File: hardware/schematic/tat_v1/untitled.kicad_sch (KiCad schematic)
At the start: 26 parts, among them J2 USB_C_Receptacle_USB2.0_14P, J3 JST-PH 2 Pin, SW6 SW_SPDT, U5 BQ25185, U6 TPS631000DRLR, U7 USBLC6-2P6

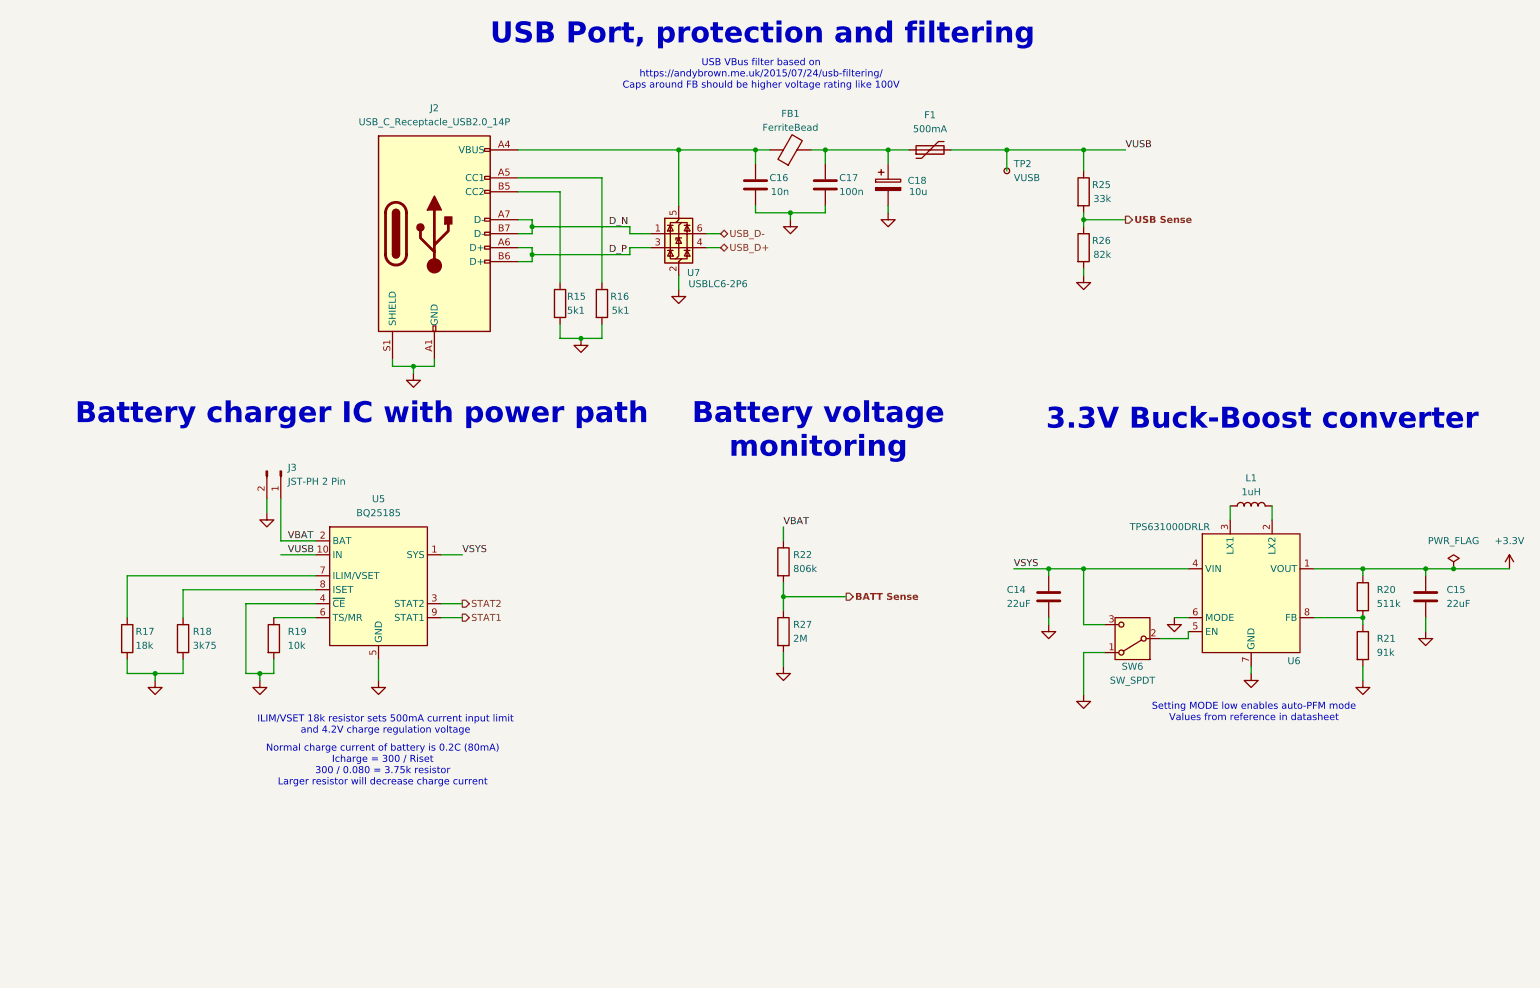
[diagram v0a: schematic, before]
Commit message: Cleaned up basic schematic and double checked all components. Need to complete ERC.
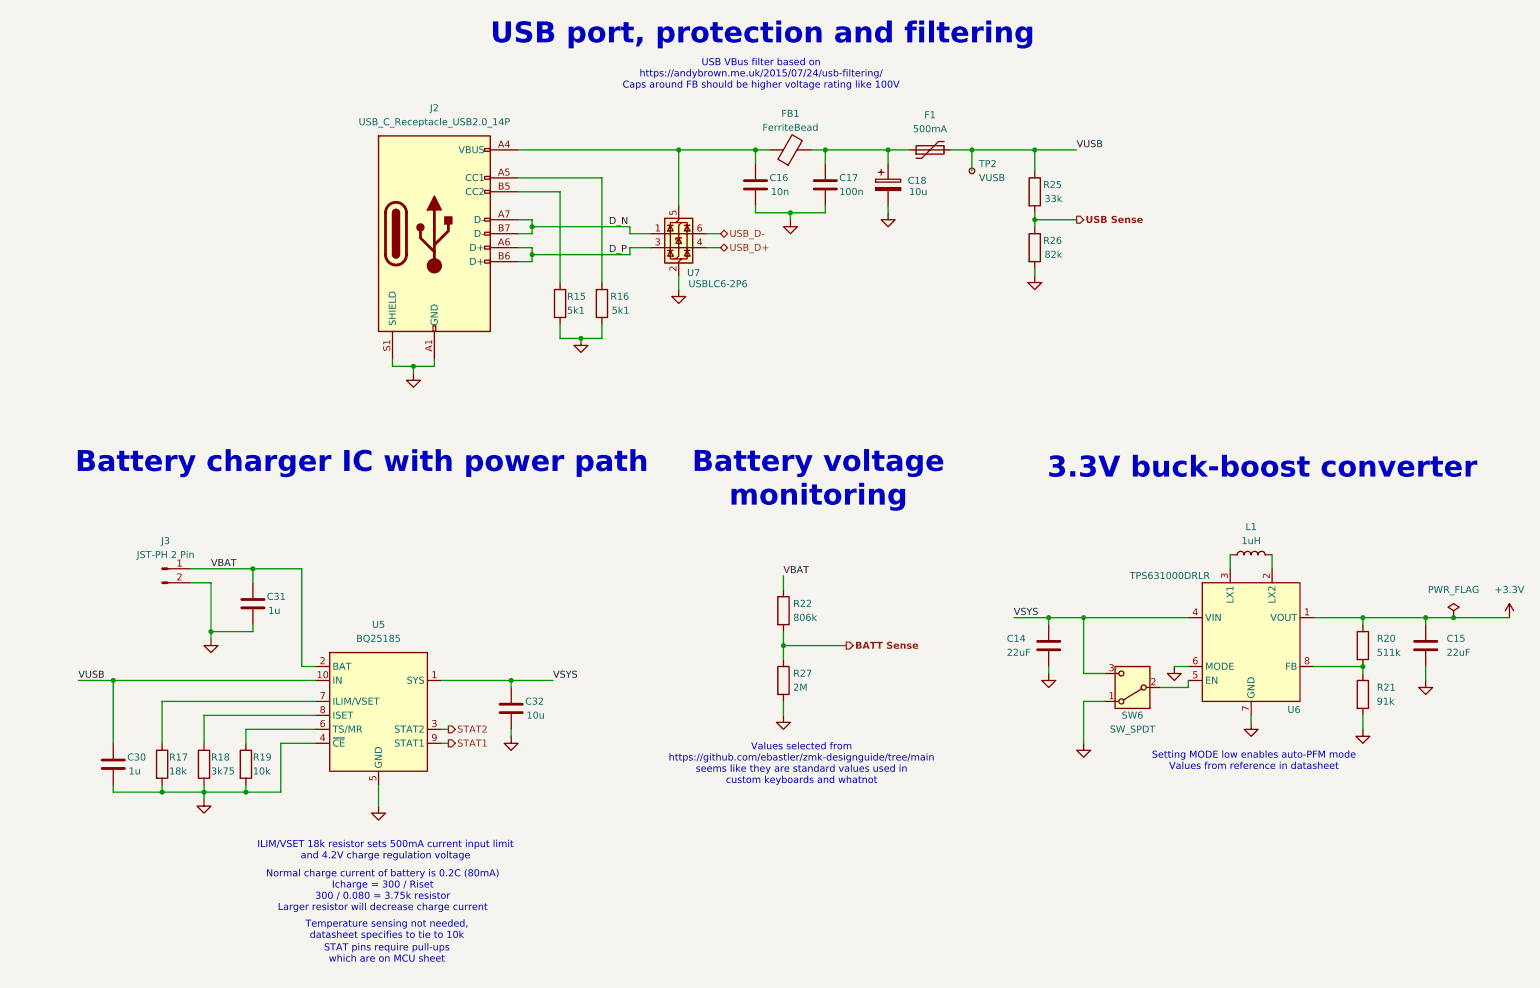
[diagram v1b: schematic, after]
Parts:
- added C30, C31: 1u, symbol Device:C
- added C32: 10u, symbol Device:C
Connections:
- net GND: now also C30.2, C31.2, C32.2
- net VBAT: now also C31.1
- net VSYS: now also C32.1
- net VUSB: now also C30.1
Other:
- note added: "3.3V buck-boost converter"
- note added: "STAT pins require pull-ups which are on MCU sheet"
- note added: "Temperature sensing not needed, datasheet specifies to tie to 10k"
- note added: "USB port, protection and filtering"
- note added: "Values selected from https://github.com/ebastler/zmk-designguide/tree/main seems like they are standard values used in custom keyboards and whatnot"
- note removed: "3.3V Buck-Boost converter"
- note removed: "USB Port, protection and filtering"
- moved on the sheet: C14, C15, J3, L1, R17, R18, R19, R20, R21, R22, R25, R26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

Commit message: Added new titles to sheets
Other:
- title: (none) -> Tiny Ambient Tracker - power
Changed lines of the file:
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@@
 	(generator_version "9.0")
 	(paper "A4")
+	(title_block
+		(title "Tiny Ambient Tracker - power")
+	)
 	(text "ILIM/VSET 18k resistor sets 500mA current input limit \nand 4.2V charge regulation voltage"
 		(exclude_from_sim no)

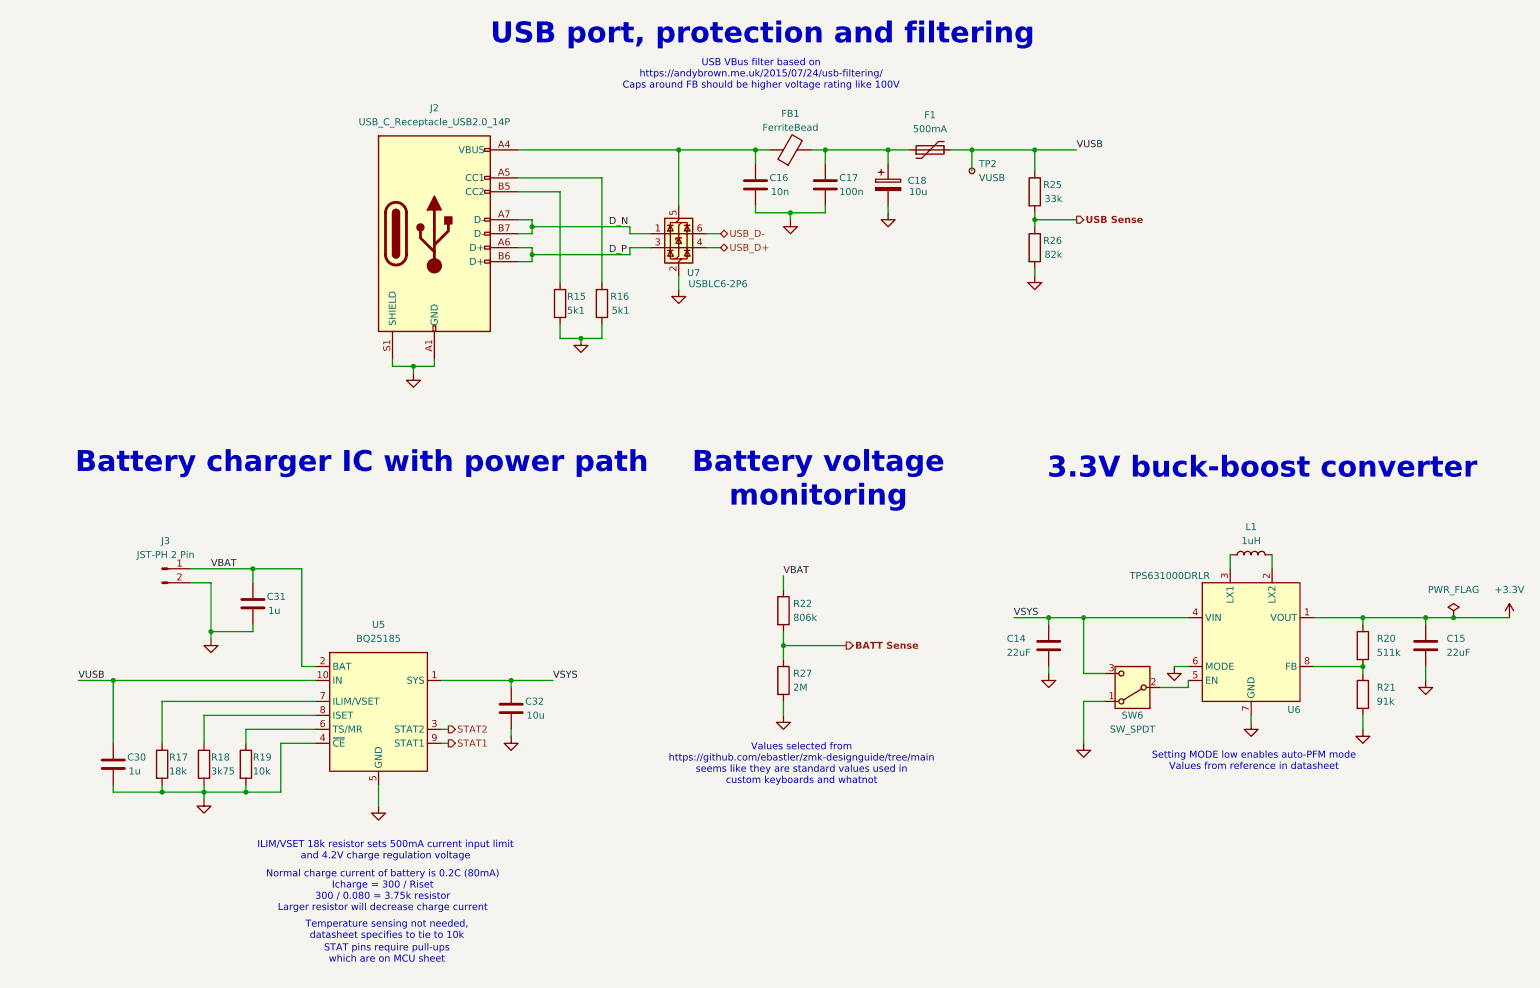
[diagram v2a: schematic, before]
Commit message: Used auto reference designator on whole schematic
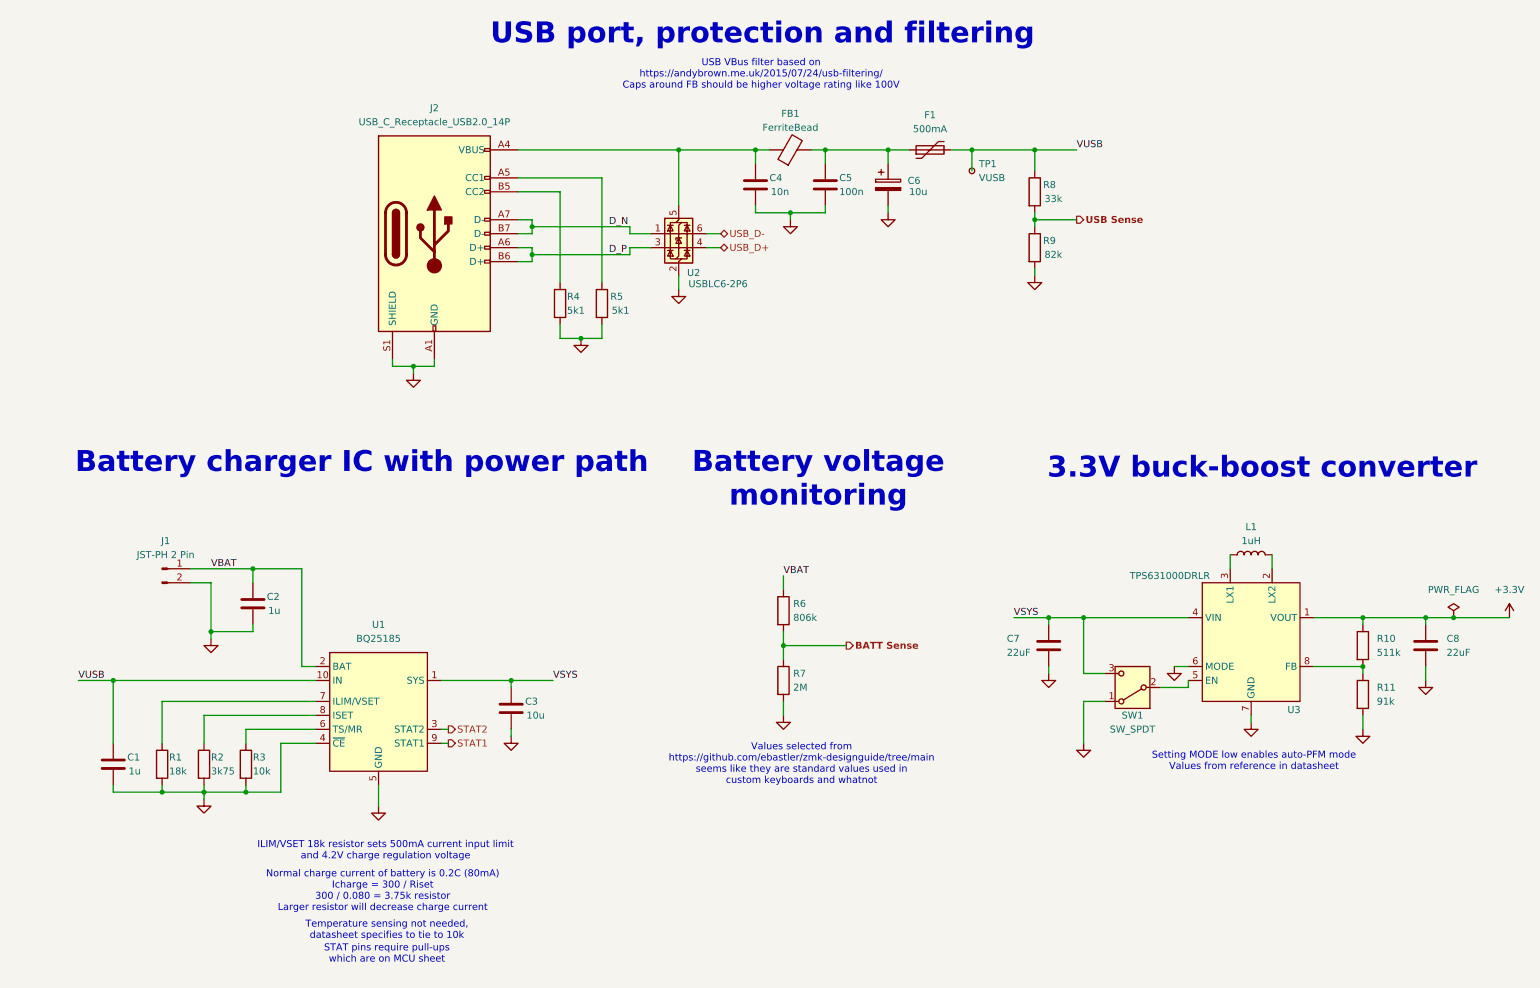
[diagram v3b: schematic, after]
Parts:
- renumbered C30 to C1, C31 to C2, C32 to C3, C16 to C4, C17 to C5, C18 to C6, C14 to C7, C15 to C8, J3 to J1, R17 to R1, R20 to R10, R21 to R11, R18 to R2, R19 to R3, R15 to R4, R16 to R5, R22 to R6, R27 to R7, R25 to R8, R26 to R9, SW6 to SW1, TP2 to TP1, U5 to U1, U7 to U2, U6 to U3

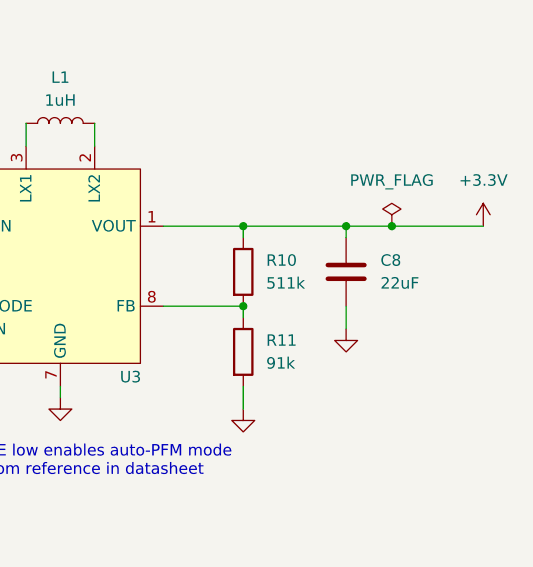
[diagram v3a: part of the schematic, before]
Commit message: Working on assigning footprints. Fixed buck-boost output capacitor using wrong value.
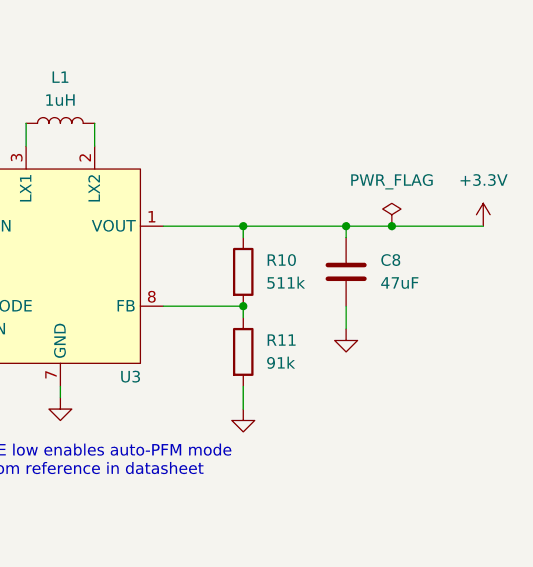
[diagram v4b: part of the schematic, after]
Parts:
- C1, C2, C3, C4, C5: footprint (none) -> Capacitor_SMD:C_0402_1005Metric
- C7: footprint (none) -> Capacitor_SMD:C_0603_1608Metric
- C8: value 22uF -> 47uF
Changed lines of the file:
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@@
 			)
 		)
-		(property "Value" "22uF"
+		(property "Value" "47uF"
 			(at 269.24 135.8899 0)
 			(effects
@@
 			)
 		)
-		(property "Footprint" ""
+		(property "Footprint" "Capacitor_SMD:C_0402_1005Metric"
 			(at 27.6352 160.02 0)
 			(effects
@@
 			)
 		)
-		(property "Footprint" ""
+		(property "Footprint" "Capacitor_SMD:C_0402_1005Metric"
 			(at 53.0352 130.81 0)
 			(effects
@@
 			)
 		)
-		(property "Footprint" ""
+		(property "Footprint" "Capacitor_SMD:C_0402_1005Metric"
 			(at 100.0252 149.86 0)
 			(effects
@@
 			)
 		)
-		(property "Footprint" ""
+		(property "Footprint" "Capacitor_SMD:C_0402_1005Metric"
 			(at 144.4752 54.61 0)
 			(effects
@@
 			)
 		)
-		(property "Footprint" ""
+		(property "Footprint" "Capacitor_SMD:C_0402_1005Metric"
 			(at 157.1752 54.61 0)
 			(effects
@@
 			)
 		)
-		(property "Footprint" ""
+		(property "Footprint" "Capacitor_SMD:C_0603_1608Metric"
 			(at 197.8152 138.43 0)
 			(effects
